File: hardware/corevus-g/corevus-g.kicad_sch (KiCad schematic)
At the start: 258 parts, among them J1 USB 2.0, J10 JST XH, J11 JST XH, J12 JST XH, J13 USB 2.0, J14 KK2.54, J15 JST XH, J16 JST XH, J17 JST XH, J18 1x3P, J19 1x3P, J2 JST XH, J20 1x3P, J21 JST XH, J22 JST XH, J23 JST XH, J24 XH, J25 XH, J26 XH, J27 JST XH, J28 MF3 2x04P, J29 USB_A, J3 1x2P, J31 1x3P, J35 1x2P, J36 1x2P, J37 JST XH, J38 1x3P, J39 JST XH, J4 JST XH, J40 JST XH, J41 1x3P, J42 1x3P, J43 1x2P, J44 1x2P, J5 JST XH, J6 KK2.54, J7 JST XH, J8 JST XH, J9 JST XH, Q1 AO3400, Q19 AO3400, Q2 AO3400, Q20 AO3400, Q21 AO3400, Q22 AO3400, Q23 AO3400, Q24 AO3400, Q25 60N03F, Q26 60N03F, Q27 AO3400, Q28 AO3400, Q29 AO3400, Q30 AO3400, SW1 SPST, SW3 SPST, U1 STM32F407ZETx, U2 CD4504B, U3 TPS54335A, U4 TPS54335A, U5 AMS1117-3.3, Y1 25 MHz

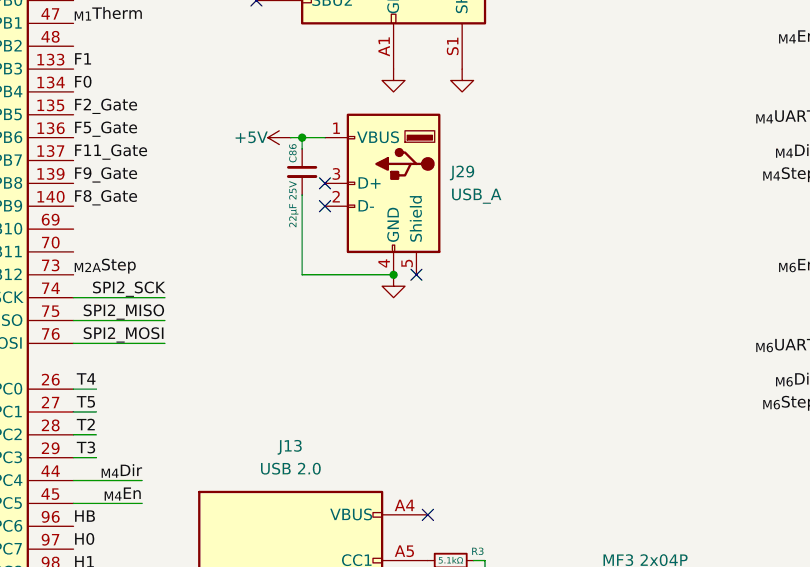
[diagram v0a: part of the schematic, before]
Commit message: Added details on fan / motor voltage selection
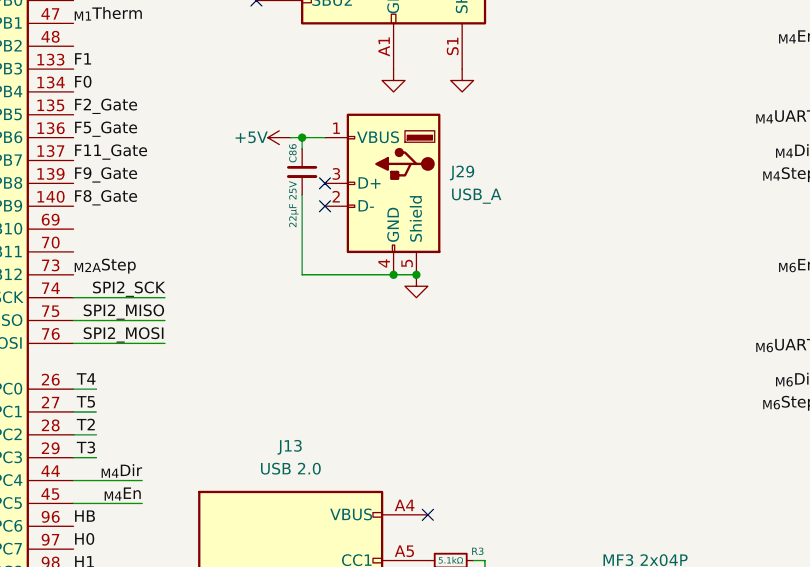
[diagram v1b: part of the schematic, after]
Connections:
- net GND: now also J29.5 (Shield)
- no-connect marks 20 -> 19
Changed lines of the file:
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@@
 	)
 	(junction
+		(at 274.32 109.22)
+		(diameter 0)
+		(color 0 0 0 0)
+	)
+	(junction
 		(at 240.03 237.49)
 		(diameter 0)
@@
 	)
 	(no_connect
-		(at 274.32 109.22)
-	)
-	(no_connect
 		(at 339.09 121.92)
 	)
@@
 	(wire
 		(pts
+			(xy 274.32 109.22) (xy 271.78 109.22)
+		)
+		(stroke
+			(width 0)
+			(type default)
+		)
+	)
+	(wire
+		(pts
 			(xy 64.77 24.13) (xy 64.77 31.75)
 		)
@@
 	(symbol
 		(lib_id "power:GND")
-		(at 271.78 109.22 0)
+		(at 274.32 109.22 0)
 		(mirror y)
 		(unit 1)
@@
 		(dnp no)
 		(property "Reference" "#PWR018"
-			(at 271.78 115.57 0)
+			(at 274.32 115.57 0)
 			(effects
 				(font
@@
 		)
 		(property "Value" "GND"
-			(at 271.78 111.76 90)
+			(at 274.32 111.76 90)
 			(effects
 				(font
@@
 		)
 		(property "Footprint" ""
-			(at 271.78 109.22 0)
+			(at 274.32 109.22 0)
 			(effects
 				(font
@@
 		)
 		(property "Datasheet" ""
-			(at 271.78 109.22 0)
+			(at 274.32 109.22 0)
 			(effects
 				(font
@@
 		)
 		(property "Description" ""
-			(at 271.78 109.22 0)
+			(at 274.32 109.22 0)
 			(effects
 				(font
